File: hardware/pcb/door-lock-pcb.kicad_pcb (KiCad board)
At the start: 2 copper layers, 77.2 x 77.2 mm, 41 parts, among them J1 105162-0001, J2 Conn_01x08, J3 Conn_01x03, J4 Conn_01x04, J7 JST XH, Q1 SI2308DS, U1 ESP32-DEVKIT-V1, U2 DS1307Z+, U3 MP1470, Y1 Crystal

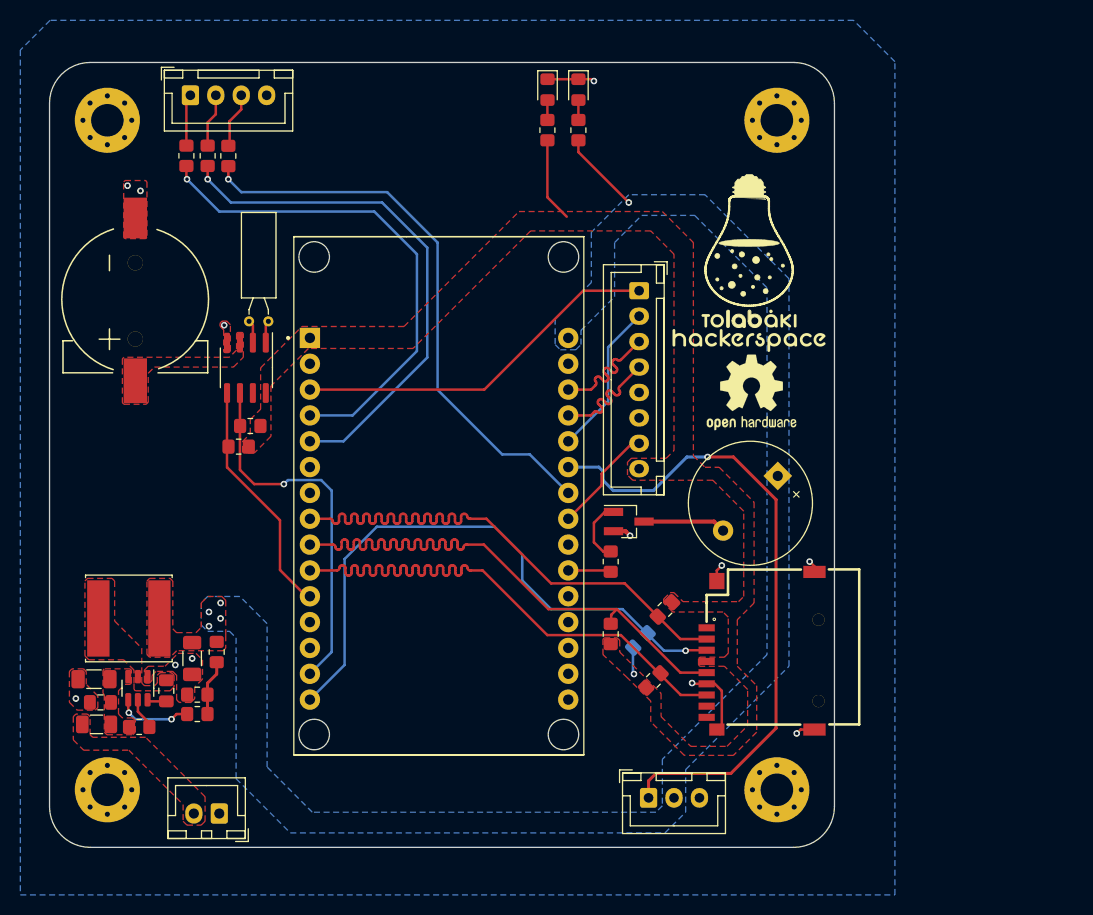
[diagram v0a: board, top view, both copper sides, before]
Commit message: added a mosfet for the solenoid + upgraded he fuse
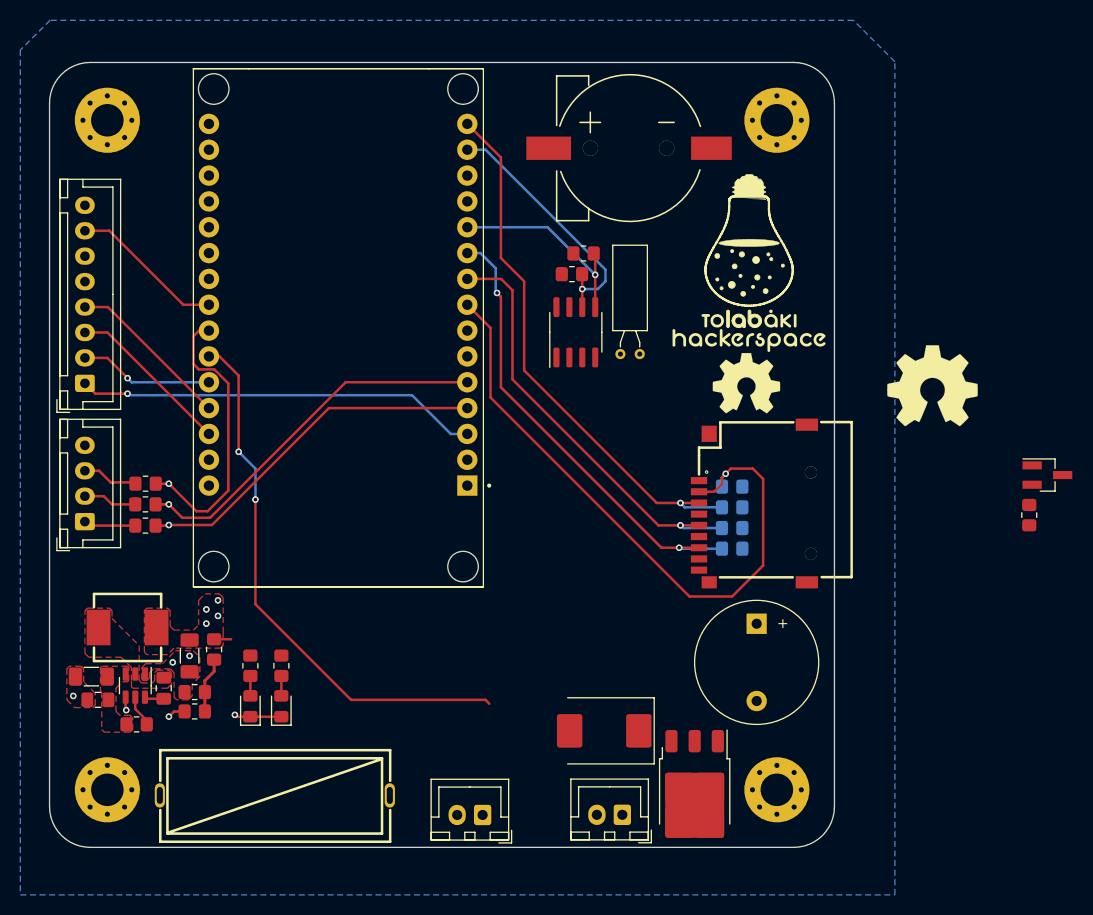
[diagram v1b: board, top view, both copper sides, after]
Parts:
- removed J3: Conn_01x03, Connector_JST:JST_XH_B3B-XH-A_1x03_P2.50mm_Vertical
- removed the REF** at (193.4, 92.5)
- added D1: ES3JBF, Diode_SMD:D_SMC, F.Cu at (178.9, 125.7)
- added J6: Conn_01x02, Connector_JST:JST_XH_B2B-XH-A_1x02_P2.50mm_Vertical, F.Cu at (180.7, 134.0)
- added Q3: DMN6068LK3, Package_TO_SOT_SMD:TO-252-3_TabPin4, F.Cu at (187.8, 131.8)
- added REF**: OSHW-Symbol_6.7x6mm_SilkScreen, Symbol:OSHW-Symbol_6.7x6mm_SilkScreen, F.Cu at (192.9, 91.6)
- added REF**: OSHW-Symbol_8.9x8mm_SilkScreen, Symbol:OSHW-Symbol_8.9x8mm_SilkScreen, F.Cu at (211.2, 91.8)
- F1: footprint Fuse:Fuse_1206_3216Metric -> C3131:FUSE-TH_L22.6-W9.0
- J7: value JST XH -> Conn_01x02
- L1: footprint Inductor_SMD:L_Changjiang_FNR8040S -> C5189755:IND-SMD_L7.2-W6.6_GPSR07X0
- R10, R15, R16: moved to B.Cu
- moved D2 68.7 mm to (144.2, 123.3), turned to 90 degrees
- moved D3 66.0 mm to (147.2, 123.3), turned to 90 degrees
- moved R11 61.7 mm to (144.2, 119.3), turned to -90 degrees
- moved R12 58.8 mm to (147.2, 119.3), turned to -90 degrees
- moved J2 55.2 mm to (127.9, 91.6), turned to 90 degrees
- moved BT1 50.9 mm to (181.5, 68.5), turned to 0 degrees
- moved J4 43.2 mm to (127.9, 105.2), turned to 90 degrees
- moved Q1 41.4 mm to (222.5, 100.6)
- moved R1 41.4 mm to (220.7, 104.5)
- moved R5 38.9 mm to (176.9, 78.8), turned to 180 degrees
- moved Y1 36.7 mm to (182.4, 88.7)
- moved R2 36.6 mm to (133.8, 105.6), turned to 180 degrees
- moved R4 35.0 mm to (175.8, 80.8), turned to 180 degrees
- moved R17 34.8 mm to (133.8, 103.5), turned to 180 degrees
- moved R3 33.2 mm to (133.9, 101.4), turned to 180 degrees
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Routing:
- net /LED_B: track 56.0 -> 28.3 mm
- net /VSPI_CLK: track 61.5 -> 42.1 mm, vias 0 -> 1
- net /LED_G: track 51.4 -> 36.7 mm
- net /VSPI_MISO: track 59.8 -> 45.6 mm, vias 0 -> 2
- net /LED_R: track 49.7 -> 35.4 mm
- net GND: track 18.5 -> 4.64 mm, vias 12 -> 4
- net /I2C_SCL: track 36.6 -> 25.5 mm
- net +3V3: track 10.9 -> 0.00 mm, vias 1 -> 0
- net /RELAY: track 63.8 -> 53.9 mm, vias 1 -> 2
- net Net-(BZ1-+): track 8.14 -> 0.00 mm
- net +5V: track 8.16 -> 1.67 mm, vias 5 -> 4
- net Net-(Q1-G): track 6.31 -> 0.00 mm
- net /VSPI_MOSI: track 58.7 -> 53.4 mm
- net Net-(U3-FB): track 7.51 -> 2.96 mm
- net /RFID_RST: track 10.7 -> 15.2 mm
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- removed copper zone on F.Cu, net +3V0
- removed copper zone on F.Cu, net +3V3
- removed copper zone on B.Cu, net +5V
- removed copper zone on F.Cu, net Net-(J7-Pin_2)

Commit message: finished rev 1 of pcb + ported MFRC522 library to ESP-IDF + finished the BOM
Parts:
- removed BZ1: Buzzer, Buzzer_Beeper:Buzzer_12x9.5RM7.6
- removed the REF** at (211.2, 91.8)
- added BUZZER1: FT12095-G/12V, C781867:BUZ-TH_BD12.0-P7.60-D0.6-FD, F.Cu at (193.9, 118.9)
- added C6: 100, Capacitor_SMD:CP_Elec_6.3x5.4, F.Cu at (160.5, 122.6)
- added C7: 100, Capacitor_SMD:CP_Elec_6.3x5.4, F.Cu at (168.7, 122.6)
- added C8: 1uf, Capacitor_SMD:C_0805_2012Metric_Pad1.18x1.45mm_HandSolder, F.Cu at (176.0, 89.9)
- added D4: ~, LED_SMD:LED_0805_2012Metric_Pad1.15x1.40mm_HandSolder, F.Cu at (177.7, 117.7)
- added Q2: BC817DPN, Package_TO_SOT_SMD:SOT-363_SC-70-6, F.Cu at (181.2, 119.8)
- added R13: 220, Resistor_SMD:R_0805_2012Metric_Pad1.20x1.40mm_HandSolder, F.Cu at (185.3, 120.1)
- added R18: 220, Resistor_SMD:R_0805_2012Metric_Pad1.20x1.40mm_HandSolder, F.Cu at (177.7, 119.8)
- added R19: 4k7, Resistor_SMD:R_0805_2012Metric_Pad1.20x1.40mm_HandSolder, F.Cu at (174.8, 118.9)
- R4, R5: moved to B.Cu
- moved Q1 38.8 mm to (186.1, 113.8)
- moved R1 37.6 mm to (185.2, 116.6), turned to 180 degrees
- moved R5 3.25 mm to (173.7, 78.1), turned to -135 degrees
- moved R10 1.79 mm to (193.3, 101.7)
- moved R14 1.79 mm to (193.3, 103.8)
- moved R15 1.79 mm to (193.3, 105.8)
- moved R16 1.79 mm to (193.3, 107.8)
- moved J7 1.52 mm to (165.5, 134.0)
- moved Y1 1.17 mm to (183.6, 88.4)
- moved U2 0.46 mm to (176.0, 86.1), turned to 180 degrees
- moved R4 0.26 mm to (175.5, 80.9)
- turned D1 to 0 degrees
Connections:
- J1 pad 2: /VSPI_CS -> /HSPI_CS
- J1 pad 3: /VSPI_MOSI -> /HSPI_MOSI
- J1 pad 5: /VSPI_CLK -> /HSPI_CLK
- J1 pad 7: /VSPI_MISO -> /HSPI_MISO
- J2 pad 1: /HSPI_CS -> /VSPI_CS
- J2 pad 2: /HSPI_CLK -> /VSPI_CLK
- J2 pad 3: /HSPI_MOSI -> /VSPI_MOSI
- J2 pad 4: /HSPI_MISO -> /VSPI_MISO
- J2 pad 5: unconnected-(J2-Pin_5-Pad5) -> /IRQ
- Q3 pad 1: unconnected-(Q3-G-Pad1) -> Net-(Q3-G)
- R10 pad 1: /VSPI_CS -> /HSPI_CS
- R14 pad 1: /VSPI_MOSI -> /HSPI_MOSI
- R15 pad 1: /VSPI_CLK -> /HSPI_CLK
- R16 pad 1: /VSPI_MISO -> /HSPI_MISO
- U1 pad 19: unconnected-(U1-D34-Pad19) -> /IRQ
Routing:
- net +3V3: track 0.00 -> 147.7 mm, vias 0 -> 4
- net /BUZZER: track 0.00 -> 118.3 mm
- net /HSPI_CLK: track 13.2 -> 58.4 mm
- net /HSPI_MISO: track 16.3 -> 58.3 mm, vias 0 -> 1
- net /HSPI_MOSI: track 16.3 -> 56.9 mm, vias 0 -> 2
- net /LED_R: track 35.4 -> 64.6 mm
- net /VSPI_MISO: track 45.6 -> 72.9 mm, vias 2 -> 1
- net /VSPI_CLK: track 42.1 -> 67.0 mm, vias 1 -> 0
- net +3V0: track 0.00 -> 23.7 mm
- net +12V: track 0.00 -> 23.4 mm
- net GND: track 4.64 -> 25.8 mm, vias 4 -> 22
- net /HSPI_CS: track 39.7 -> 58.6 mm
- net /LED_G: track 36.7 -> 54.2 mm
- net /IRQ: track 0.00 -> 15.5 mm
- net /VSPI_MOSI: track 53.4 -> 67.1 mm, vias 1 -> 0
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- added copper zone on F.Cu, net Net-(D1-A)
- added copper zone on F.Cu, net Net-(J6-Pin_1)
- added copper zone on F.Cu, net Net-(J7-Pin_2)

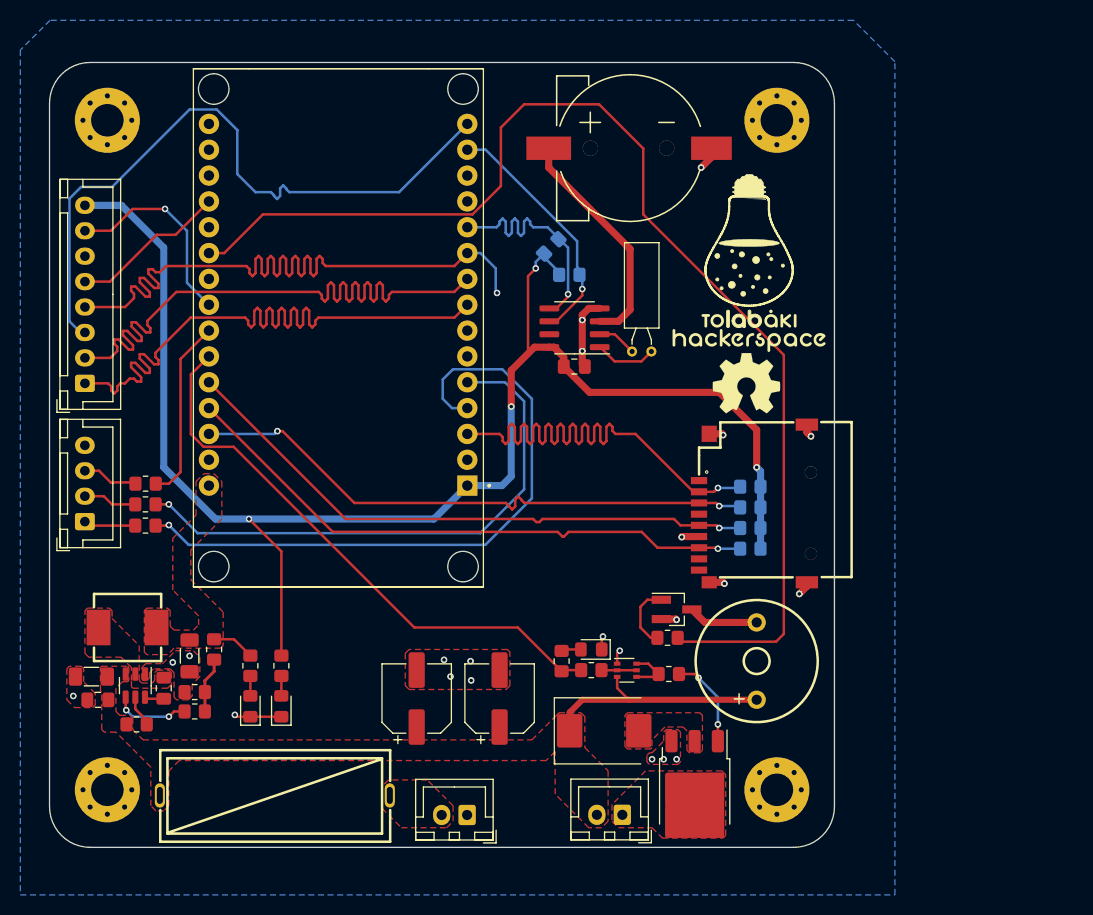
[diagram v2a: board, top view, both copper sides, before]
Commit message: changed mosfet driver + connected sd to pwr
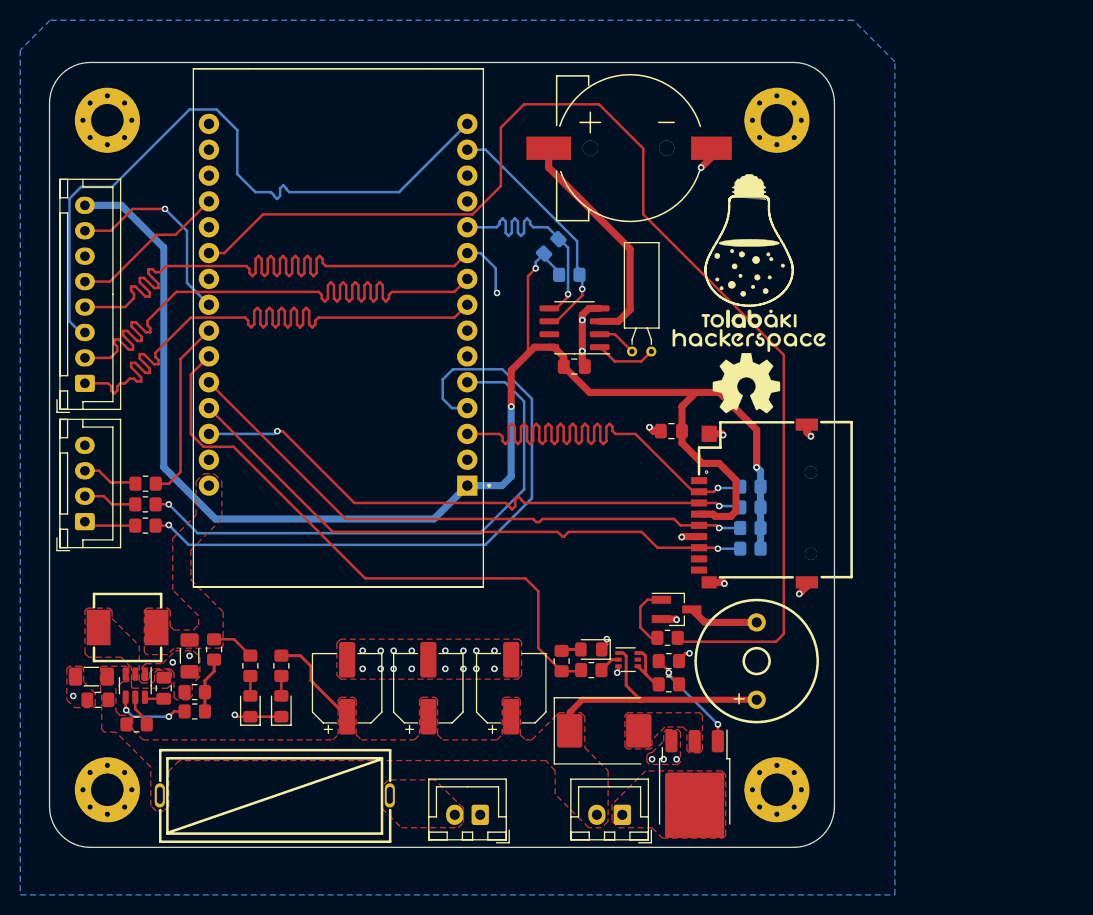
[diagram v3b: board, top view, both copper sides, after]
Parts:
- removed Q2: BC817DPN, Package_TO_SOT_SMD:SOT-363_SC-70-6
- added C5: 100, Capacitor_SMD:CP_Elec_6.3x5.4, F.Cu at (153.7, 121.5)
- added C9: 1uf, Capacitor_SMD:C_0805_2012Metric_Pad1.18x1.45mm_HandSolder, F.Cu at (185.5, 96.3)
- added R20: 220, Resistor_SMD:R_0805_2012Metric_Pad1.20x1.40mm_HandSolder, F.Cu at (185.3, 118.9)
- added U4: ZXGD3009DYTA, Package_TO_SOT_SMD:SOT-363_SC-70-6, F.Cu at (181.3, 118.7)
- R12: value 4k7 -> 10k
- moved C6 1.53 mm to (161.6, 121.5)
- moved C7 1.53 mm to (169.8, 121.5)
- moved J7 1.29 mm to (166.8, 134.0)
- moved R13 1.02 mm to (185.3, 121.2)
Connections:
- J1 pad 4: +3.3V -> +3V3
- R12 pad 1: +3V3 -> +12V
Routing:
- net +12V: track 23.4 -> 36.4 mm
- net +3V3: track 147.7 -> 152.3 mm, vias 4 -> 3
- net /RELAY: track 56.4 -> 59.9 mm
- net Net-(Q3-G): track 9.09 -> 12.0 mm
- net GND: track 25.8 -> 27.6 mm, vias 22 -> 36
- net Net-(U4-IN): track 3.45 -> 2.10 mm
- net Net-(U4-SINK): track 4.90 -> 5.53 mm

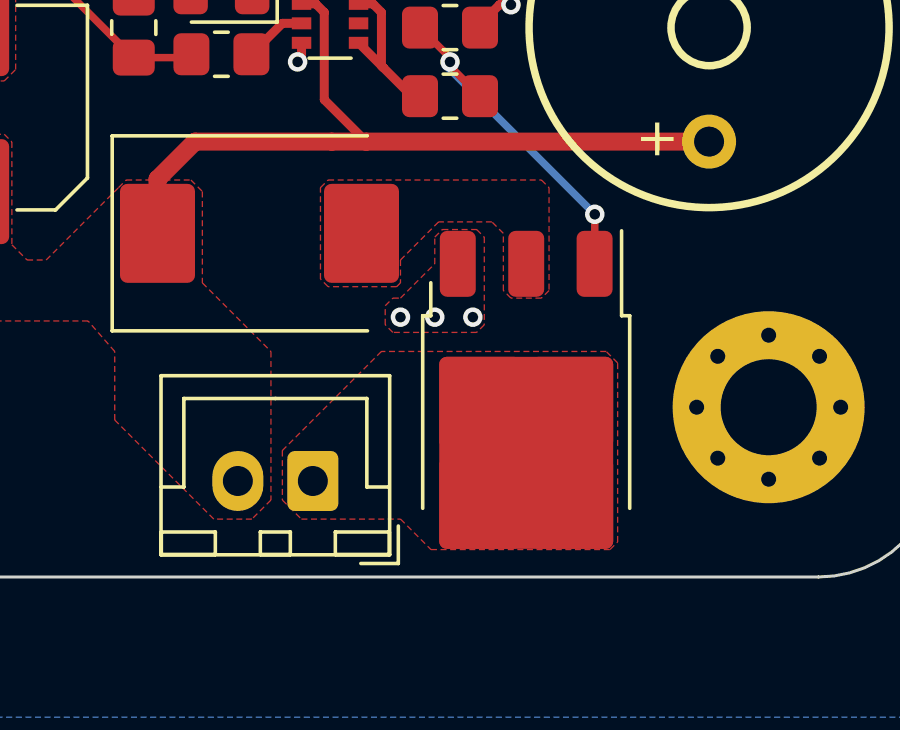
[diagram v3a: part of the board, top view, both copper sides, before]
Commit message: fixed error with mosfet drain
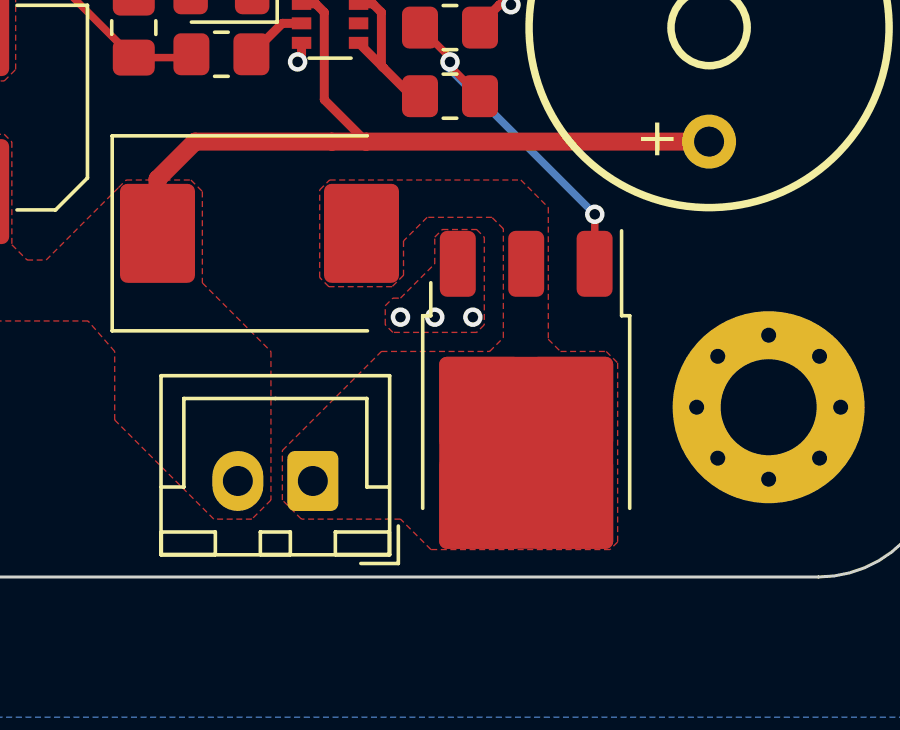
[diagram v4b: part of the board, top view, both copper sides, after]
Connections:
- J6 pad 1: Net-(J6-Pin_1) -> Net-(D1-A)
- Q3 pad 4: Net-(J6-Pin_1) -> Net-(D1-A)
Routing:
- removed copper zone on F.Cu, net Net-(J6-Pin_1)
